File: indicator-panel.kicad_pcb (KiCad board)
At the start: 2 copper layers, 133.1 x 77.2 mm, 89 parts, among them J101 Power In, J102 GND, J103 GND, P101 Data in, P102 Data Out, P103 Power In, P104 Power Out, U101 MAX3094E, U102 STP16CP05, U103 STP16CP05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

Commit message: Touch up some dates.
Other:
- board text added: "Vintage Computer Engineering Indicator Panel IP101 v 2.0 2018-01-27"
- board text removed: "Vintage Computer Engineering Indicator Panel IP101 v 2.0 2016-02-21"
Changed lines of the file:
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@@
   (title_block
     (title "Indicator Panel")
-    (date 2016-02-23)
+    (date 2018-01-27)
     (rev 2.0)
     (company "Vintage Computer Engineering")
@@
     (aux_axis_origin 0 0)
     (grid_origin 61.468 62.484)
-    (visible_elements FFFFFF7F)
+    (visible_elements FFFFEF7F)
     (pcbplotparams
       (layerselection 0x010f0_80000001)
@@
     (descr http://www.cui.com/product/resource/pj-032b.pdf)
     (tags "barrell jack 2.5mm")
-    (fp_text reference J101 (at 5.334 -9.398 180) (layer B.SilkS)
+    (fp_text reference J101 (at 5.207 -10.287 180) (layer B.SilkS)
       (effects (font (size 1 1) (thickness 0.15)) (justify mirror))
     )
-    (fp_text value "Power In" (at 2.667 -10.795 180) (layer B.SilkS)
+    (fp_text value "Power In" (at 2.413 -11.684 180) (layer B.SilkS)
       (effects (font (size 1 1) (thickness 0.15)) (justify mirror))
     )
@@
     (descr "Through hole pin header")
     (tags "pin header")
-    (fp_text reference P101 (at -4.064 0.127 180) (layer B.SilkS)
+    (fp_text reference P101 (at -5.461 0 180) (layer B.SilkS)
       (effects (font (size 1 1) (thickness 0.15)) (justify mirror))
     )
-    (fp_text value "Data in" (at -6.096 -4.572 180) (layer B.SilkS)
+    (fp_text value "Data in" (at -6.604 -3.302 180) (layer B.SilkS)
       (effects (font (size 1 1) (thickness 0.15)) (justify mirror))
     )
@@
     (descr "Through hole socket strip")
     (tags "socket strip")
-    (fp_text reference P102 (at 0 4.445 360) (layer B.SilkS)
+    (fp_text reference P102 (at 0 5.842 360) (layer B.SilkS)
       (effects (font (size 1 1) (thickness 0.15)) (justify mirror))
     )
-    (fp_text value "Data Out" (at 4.826 5.588 360) (layer B.SilkS)
+    (fp_text value "Data Out" (at 4.191 7.112 360) (layer B.SilkS)
       (effects (font (size 1 1) (thickness 0.15)) (justify mirror))
     )
@@
     (descr "Through hole pin header")
     (tags "pin header")
-    (fp_text reference P103 (at -4.064 0.889 180) (layer B.SilkS)
+    (fp_text reference P103 (at -6.477 0.127 180) (layer B.SilkS)
       (effects (font (size 1 1) (thickness 0.15)) (justify mirror))
     )
-    (fp_text value "Power In" (at -5.334 -3.048 180) (layer B.SilkS)
+    (fp_text value "Power In" (at -7.62 -3.937 180) (layer B.SilkS)
       (effects (font (size 1 1) (thickness 0.15)) (justify mirror))
     )
@@
     (descr "Through hole socket strip")
     (tags "socket strip")
-    (fp_text reference P104 (at 0 4.445 360) (layer B.SilkS)
+    (fp_text reference P104 (at 0 6.477 360) (layer B.SilkS)
       (effects (font (size 1 1) (thickness 0.15)) (justify mirror))
     )
-    (fp_text value "Power Out" (at 3.937 6.096 360) (layer B.SilkS)
+    (fp_text value "Power Out" (at 3.937 8.255 360) (layer B.SilkS)
       (effects (font (size 1 1) (thickness 0.15)) (justify mirror))
     )
@@
       (solder_mask_margin 0.77) (clearance 0.77))
   )
-  (gr_text "Vintage Computer Engineering\nIndicator Panel\nIP101  v 2.0\n2016-02-21" (at 122.555 115.951) (layer B.SilkS)
+  (gr_text "Vintage Computer Engineering\nIndicator Panel\nIP101  v 2.0\n2018-01-27" (at 122.555 115.951) (layer B.SilkS)
     (effects (font (size 1.5 1.5) (thickness 0.3)) (justify mirror))
   )

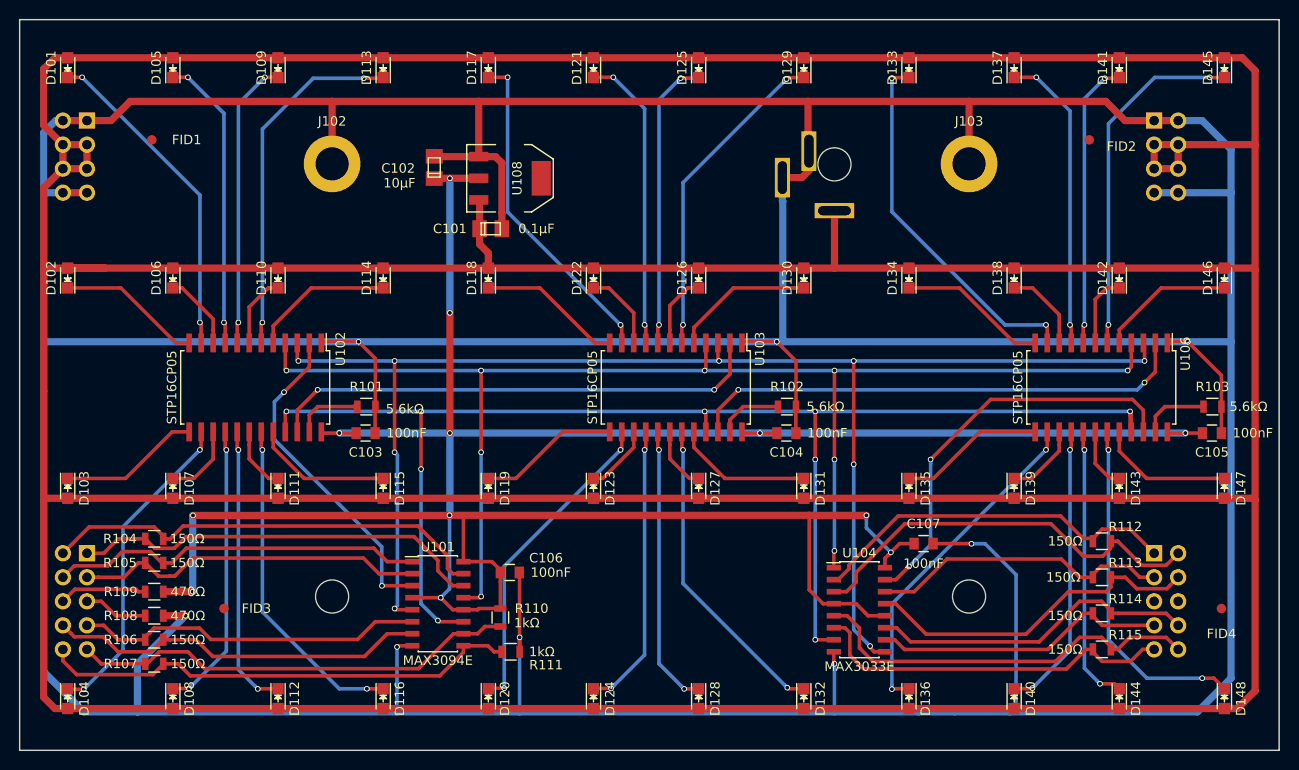
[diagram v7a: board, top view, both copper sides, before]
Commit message: Finalized v2 signal layout and submitted first batch for production.
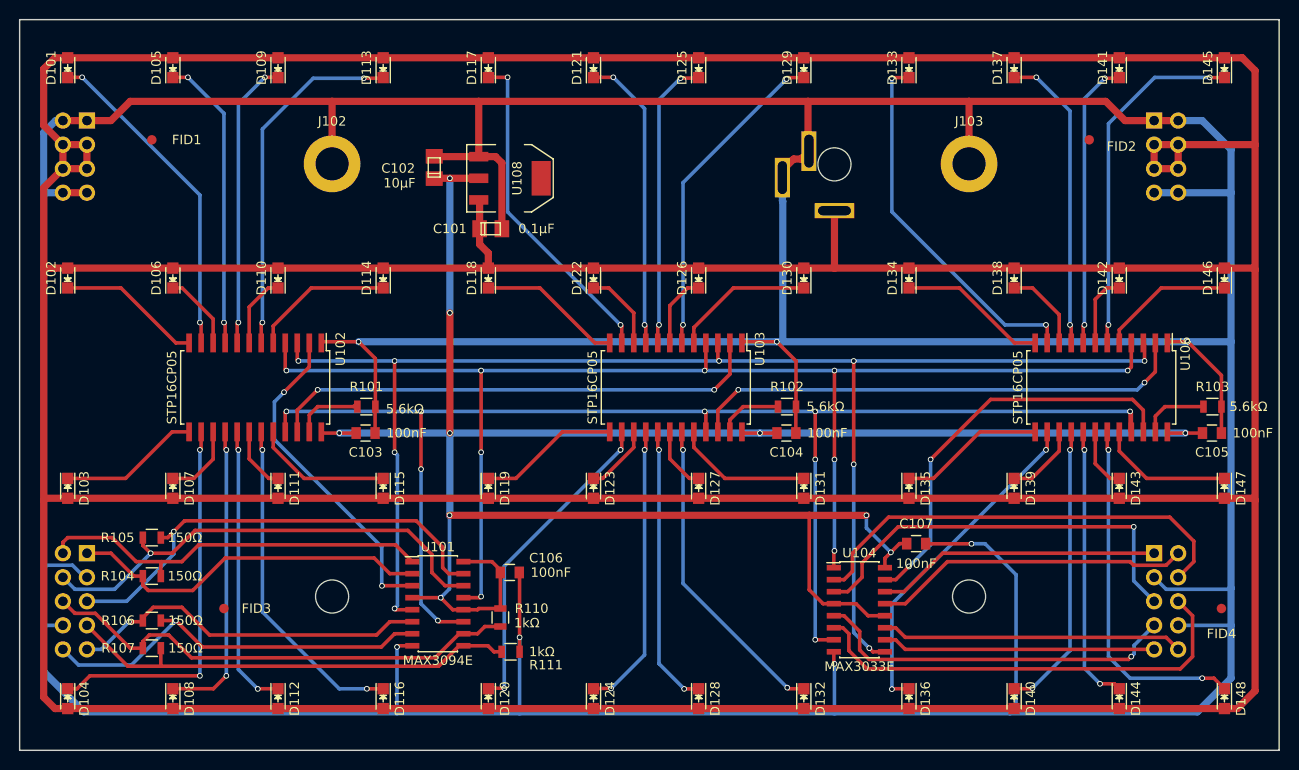
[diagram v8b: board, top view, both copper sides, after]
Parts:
- removed R108, R109: 470Ω, Resistors_SMD:R_0805
- removed R112, R113, R114, R115: 150Ω, Resistors_SMD:R_0805
- J101: value Power In -> Power In (+12V)
- P103: value Power In -> Power
- P104: value Power Out -> Power
- U108: value LD1117S33CTR -> SPX1117M3-L-3-3
- moved R104 3.95 mm to (70.4, 116.2)
- moved R105 2.68 mm to (70.4, 112.1)
- moved R106 2.05 mm to (70.4, 120.9)
- moved R107 1.67 mm to (70.4, 123.8)
- moved C107 0.78 mm to (151.1, 112.8)
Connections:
- P101 pad 3: Net-(P101-Pad3) -> GND
- P101 pad 8: Net-(P101-Pad8) -> GND
- P102 pad 3: Net-(P102-Pad3) -> GND
- P102 pad 8: Net-(P102-Pad8) -> GND
- R105 pad 1: Net-(P101-Pad3) -> Net-(P101-Pad4)
- R105 pad 2: Net-(P101-Pad4) -> Net-(P101-Pad5)
- R106 pad 1: Net-(P101-Pad7) -> Net-(P101-Pad9)
- R106 pad 2: Net-(P101-Pad8) -> Net-(P101-Pad10)
- R107 pad 1: Net-(P101-Pad9) -> Net-(P101-Pad6)
- R107 pad 2: Net-(P101-Pad10) -> Net-(P101-Pad7)
- R110 pad 2: Net-(P101-Pad9) -> Net-(P101-Pad6)
- R111 pad 1: Net-(P101-Pad10) -> Net-(P101-Pad7)
- U101 pad 1: Net-(P101-Pad4) -> Net-(P101-Pad2)
- U101 pad 10: Net-(P101-Pad9) -> Net-(P101-Pad6)
- U101 pad 14: Net-(P101-Pad1) -> Net-(P101-Pad4)
- U101 pad 15: Net-(P101-Pad2) -> Net-(P101-Pad5)
- U101 pad 2: Net-(P101-Pad3) -> Net-(P101-Pad1)
- U101 pad 6: Net-(P101-Pad7) -> Net-(P101-Pad9)
- U101 pad 7: Net-(P101-Pad8) -> Net-(P101-Pad10)
- U101 pad 9: Net-(P101-Pad10) -> Net-(P101-Pad7)
- U104 pad 10: Net-(P102-Pad7) -> Net-(P102-Pad9)
- U104 pad 11: Net-(P102-Pad8) -> Net-(P102-Pad10)
- U104 pad 13: Net-(P102-Pad4) -> Net-(P102-Pad2)
- U104 pad 14: Net-(P102-Pad3) -> Net-(P102-Pad1)
- U104 pad 2: Net-(P102-Pad1) -> Net-(P102-Pad4)
- U104 pad 3: Net-(P102-Pad2) -> Net-(P102-Pad5)
- U104 pad 5: Net-(P102-Pad10) -> Net-(P102-Pad7)
- U104 pad 6: Net-(P102-Pad9) -> Net-(P102-Pad6)
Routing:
- net Net-(P102-Pad6): track 0.00 -> 47.8 mm
- net Net-(P102-Pad5): track 0.00 -> 44.2 mm, vias 0 -> 1
- net +3V3: track 282.3 -> 238.3 mm, vias 12 -> 10
- net Net-(P101-Pad5): track 6.79 -> 49.9 mm, vias 0 -> 1
- net Net-(P101-Pad6): track 9.34 -> 51.6 mm
- net Net-(P101-Pad8): track 40.3 -> 0.00 mm
- net Net-(P101-Pad3): track 37.1 -> 0.00 mm
- net Net-(P102-Pad8): track 34.6 -> 0.00 mm
- net Net-(P102-Pad3): track 31.8 -> 0.00 mm
- net GND: track 683.0 -> 656.6 mm, vias 8 -> 7
- net Net-(P101-Pad7): track 37.0 -> 48.7 mm
- net Net-(P102-Pad4): track 36.4 -> 47.9 mm
- net Net-(P101-Pad4): track 39.8 -> 51.0 mm, vias 0 -> 1
- net Net-(P102-Pad2): track 44.1 -> 33.5 mm
- net Net-(P102-Pad10): track 42.4 -> 31.9 mm
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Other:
- board text added: "Vintage Computer Engineering Indicator Panel IP101 v 2.0 2018-02-23"
- board text removed: "Vintage Computer Engineering Indicator Panel IP101 v 2.0 2018-01-27"
